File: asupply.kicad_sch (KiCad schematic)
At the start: 98 parts, among them U10 LT3081xDF, U11 LT3042xMSE, U12 LT3045xMSE, U13 LT3045xMSE, U14 LT3042xMSE, U15 LT3094xMSE, U16 LT3042xMSE, U9 LTC3261

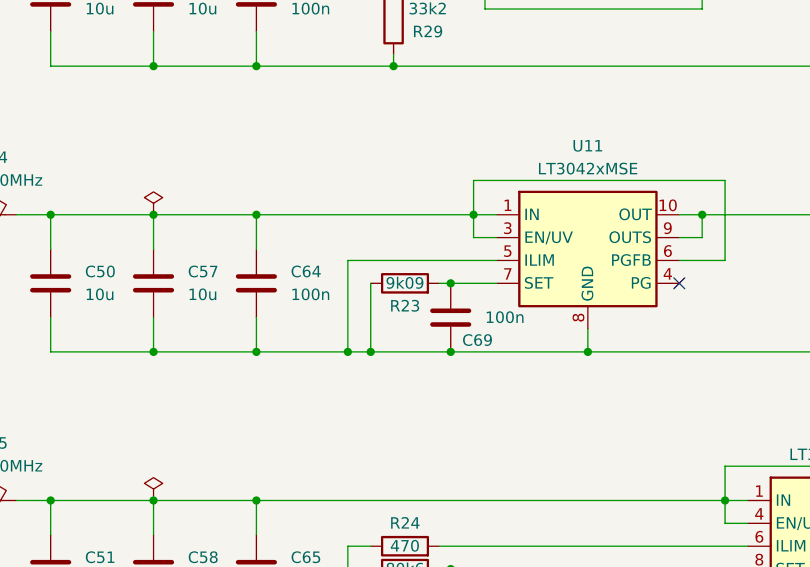
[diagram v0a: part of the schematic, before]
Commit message: sch: Fix Issue #15
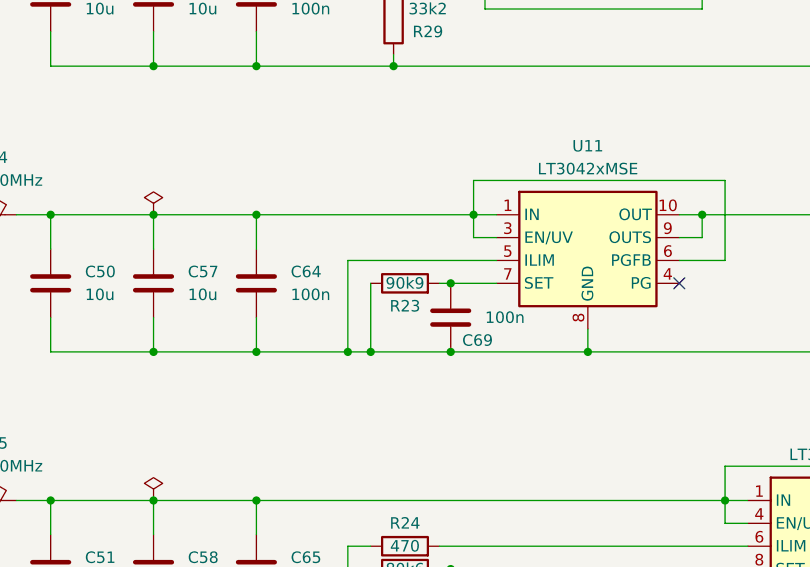
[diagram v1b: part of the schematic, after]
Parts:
- R23: value 9k09 -> 90k9; MFR_PN CR0603-FX-9091ELF -> RT0603FRE0790K9L
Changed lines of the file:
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@@
       (effects (font (size 1.27 1.27)))
     )
-    (property "Value" "9k09" (at 203.2 83.82 90)
+    (property "Value" "90k9" (at 203.2 83.82 90)
       (effects (font (size 1.27 1.27)))
     )
@@
       (effects (font (size 1.27 1.27)) hide)
     )
-    (property "MFR_PN" "CR0603-FX-9091ELF" (at 203.2 83.82 0)
+    (property "MFR_PN" "RT0603FRE0790K9L" (at 203.2 83.82 0)
       (effects (font (size 1.27 1.27)) hide)
     )

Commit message: sch: Fix Issue #14
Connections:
- net GND: now also R99.2; no longer R99.1
- net LD_EN: now also R99.1, U12.4 (EN/UV); no longer R99.2, U12.5 (PG)
- net at C51.1, C58.1, C65.1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: no longer U12.4 (EN/UV)
- no-connect marks 7 -> 8
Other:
- moved on the sheet: C51, C58, C65, C77, C84, C91, FB5

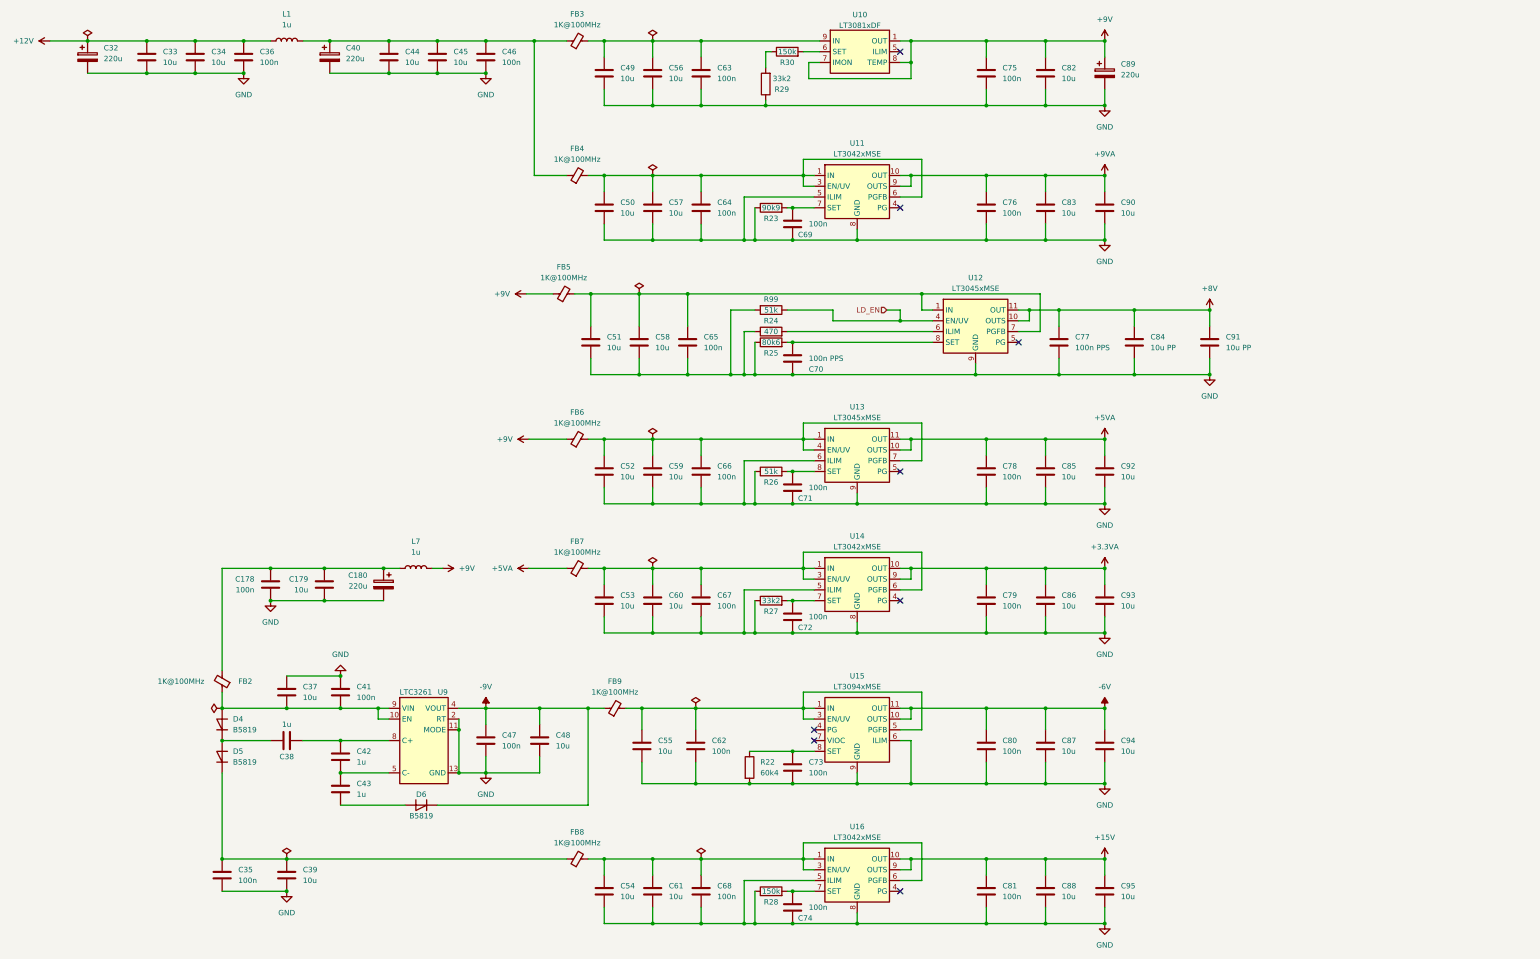
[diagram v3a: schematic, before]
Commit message: pcb: Finish Layout for rev0_3 - Assign MFR_PN for all Components - schematics changes:   - drivestage: Add Switch to optionally enable Modulation Signal Termination   -             Add alternate Precision Power Resistor   -             Modify the RC network values at TIA LPF Output   - MCU: Add Redundant 2.54mm pitch Programming Header   - thermostat: Duplicate the power filter network for alternate Temperature ADC
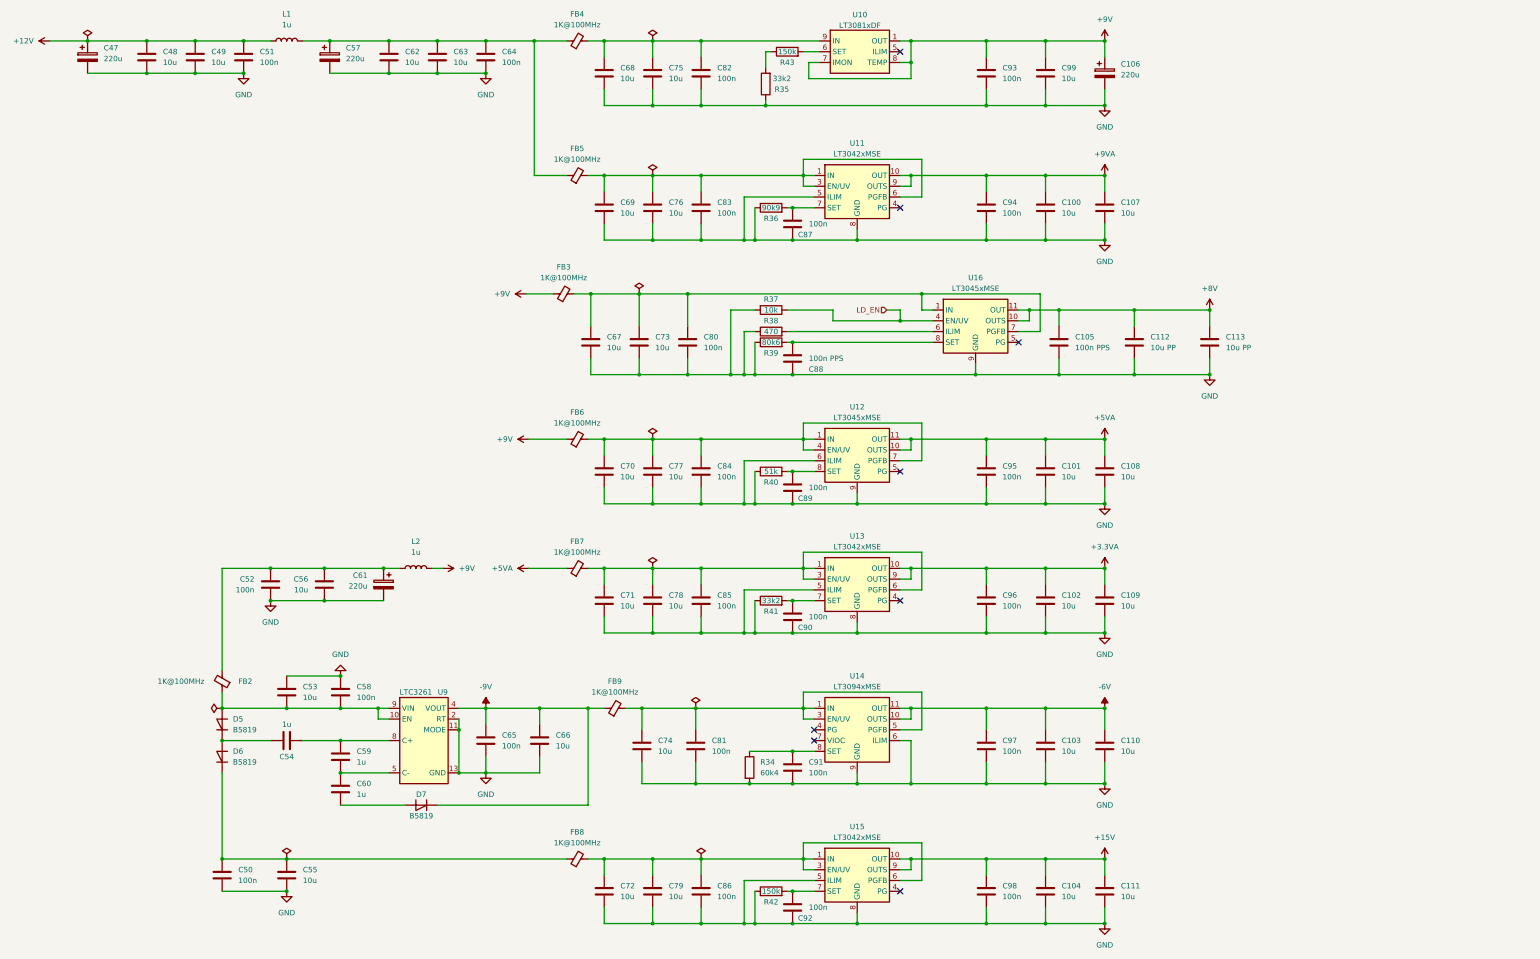
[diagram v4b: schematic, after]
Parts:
- R37: renamed from R99; value 51k -> 10k; MFR_PN RMCF0603FT51K0 -> RNCP0603FTD10K0; MFR_PN_ALT CR0603-FX-5102ELF -> RMCF0603FT10K0
- renumbered C83 to C100, C85 to C101, C86 to C102, C87 to C103, C88 to C104, C77 to C105, C89 to C106, C90 to C107, C92 to C108, C93 to C109, C94 to C110, C95 to C111, C84 to C112, C91 to C113, C32 to C47, C33 to C48, C34 to C49, C35 to C50, C36 to C51, C178 to C52, C37 to C53, C38 to C54, C39 to C55, C179 to C56, C40 to C57, C41 to C58, C42 to C59, C43 to C60, C180 to C61, C44 to C62, C45 to C63, C46 to C64, C47 to C65, C48 to C66, C51 to C67, C49 to C68, C50 to C69, C52 to C70, C53 to C71, C54 to C72, C58 to C73, C55 to C74, C56 to C75, C57 to C76, C59 to C77, C60 to C78, C61 to C79, C65 to C80, C62 to C81, C63 to C82, C64 to C83, C66 to C84, C67 to C85, C68 to C86, C69 to C87, C70 to C88, C71 to C89, C72 to C90, C73 to C91, C74 to C92, C75 to C93, C76 to C94, C78 to C95, C79 to C96, C80 to C97, C81 to C98, C82 to C99, D4 to D5, D5 to D6, D6 to D7, FB5 to FB3, FB3 to FB4, FB4 to FB5, L7 to L2, R22 to R34, R29 to R35, R23 to R36, R24 to R38, R25 to R39, R26 to R40, R27 to R41, R28 to R42, R30 to R43, U13 to U12, U14 to U13, U15 to U14, U16 to U15, U12 to U16

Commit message: sch: Update Title Block Info - rev0.3 -> rev0_3 - Correct the title of each schematics - Update the modified time
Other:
- company: M-Labs -> M-Labs Limited
- title: Kirdy -> analog supply
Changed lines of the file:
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@@
   (paper "A3")
   (title_block
-    (title "Kirdy")
-    (date "2022-07-03")
-    (rev "r0.3")
-    (company "M-Labs")
+    (title "analog supply")
+    (date "2023-11-09")
+    (rev "r0_3")
+    (company "M-Labs Limited")
     (comment 1 "Linus Woo Chun Kit")
   )

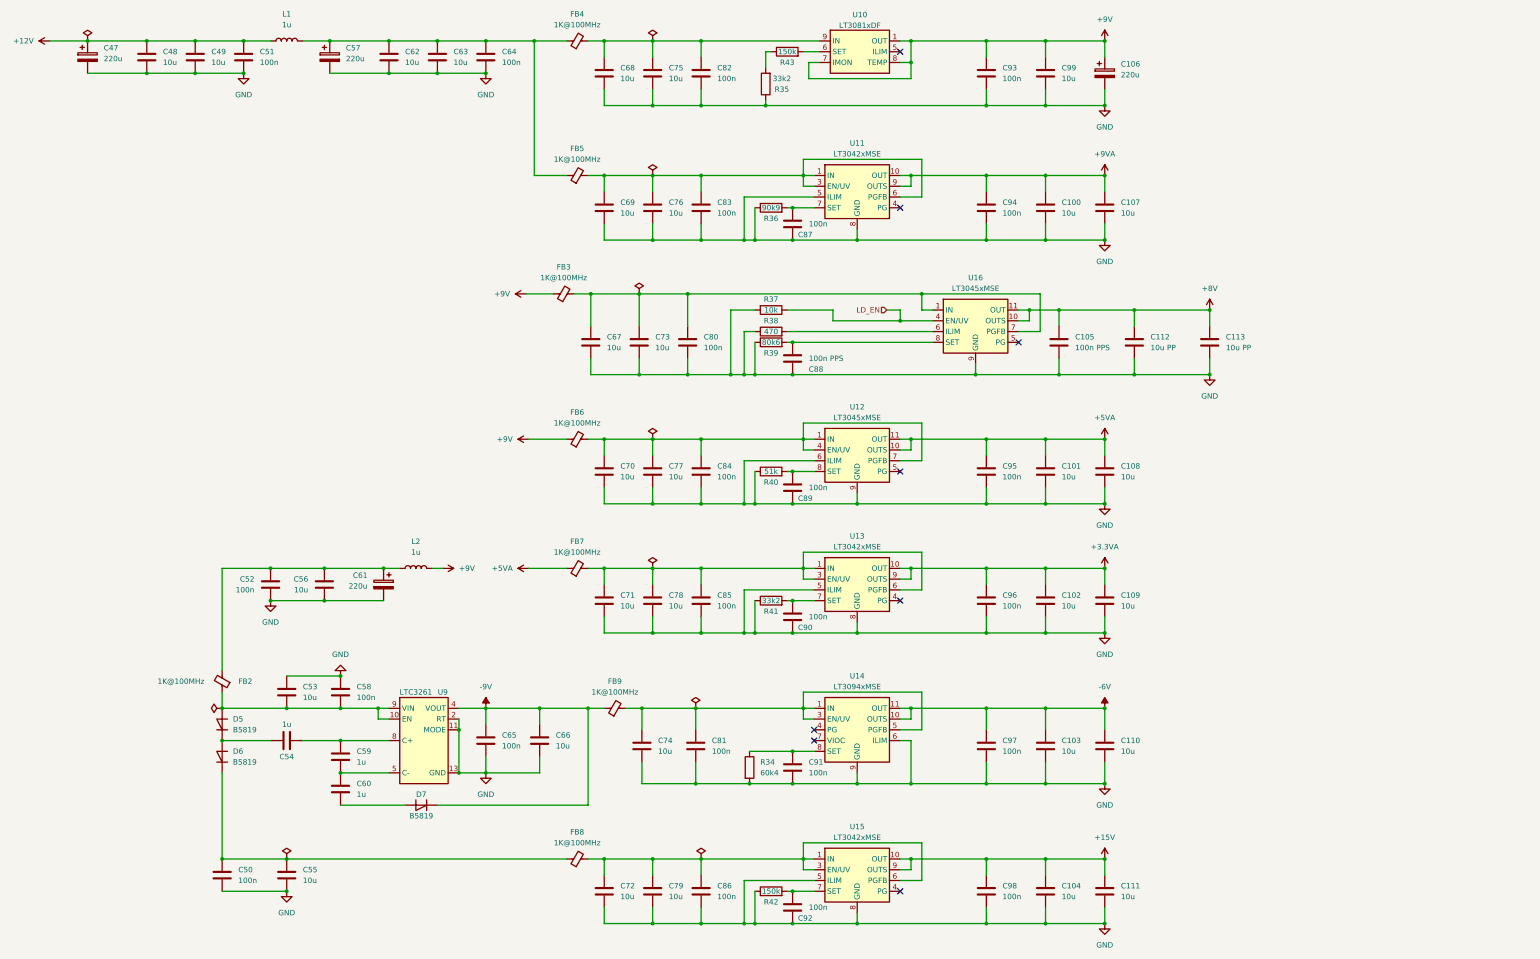
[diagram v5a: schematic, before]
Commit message: sch, pcb: Correct MFR/PN and optimize BOM
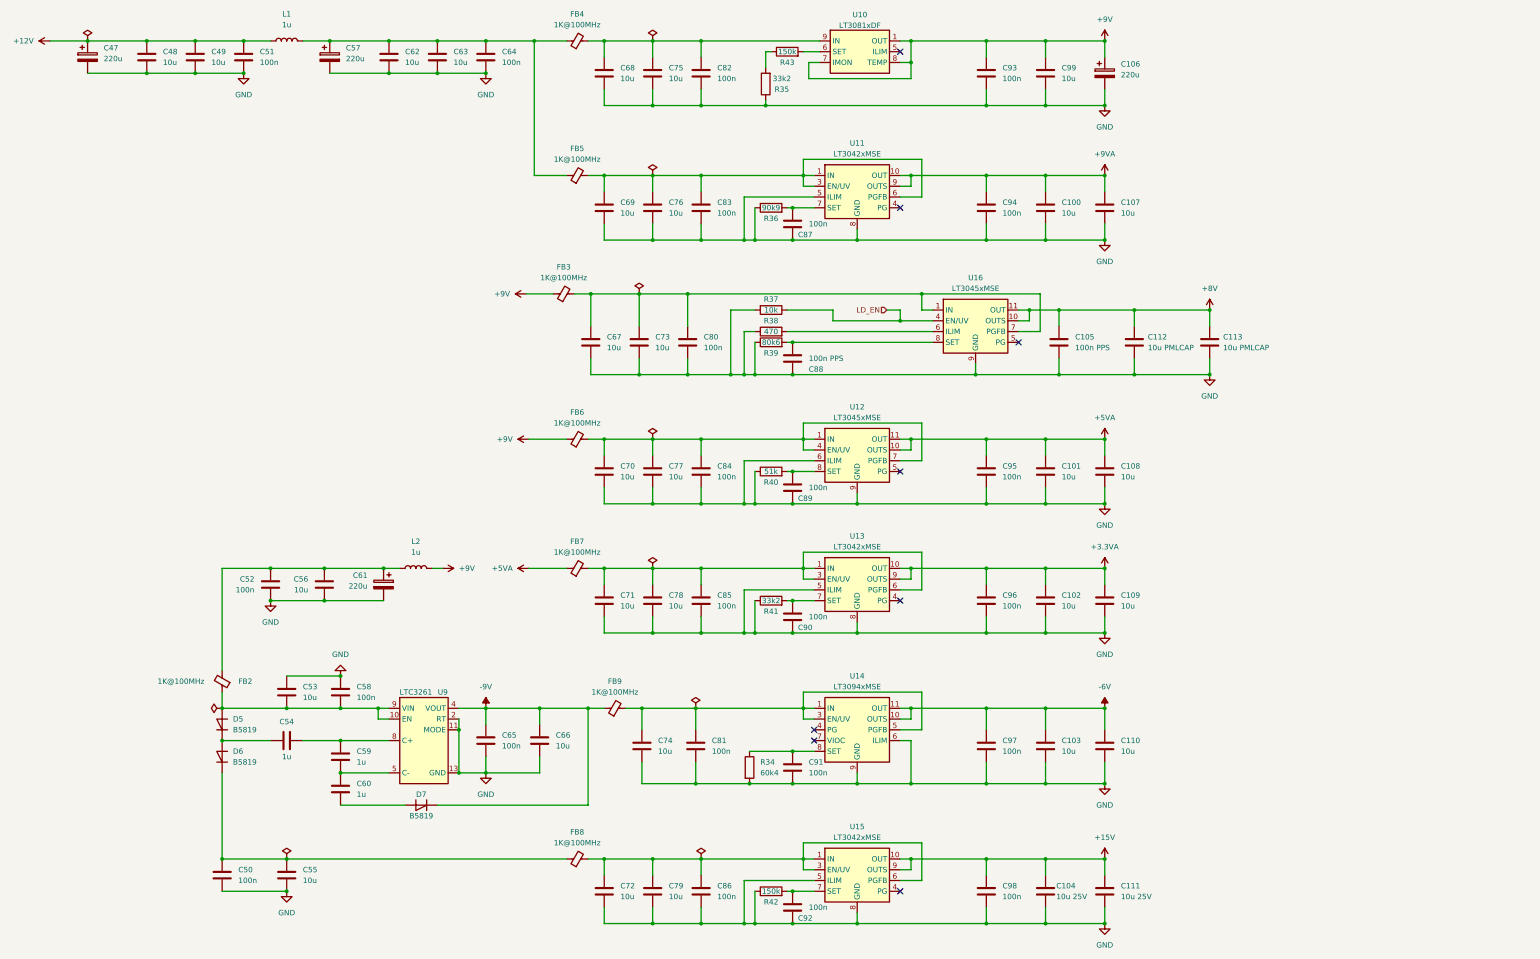
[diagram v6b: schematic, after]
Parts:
- C104, C111: value 10u -> 10u 25V; MFR_PN CL21B106KOQNNNG -> GRM21BZ71E106KE15K; MFR_PN_ALT CL21B106KOQNNNE -> GRM21BZ71E106KE15L
- C110: MFR_PN CL21B106KOQNNNG -> GRM21BZ71E106KE15K; MFR_PN_ALT CL21B106KOQNNNE -> GRM21BZ71E106KE15L
- C112, C113: value 10u PP -> 10u PMLCAP
- R36: MFR_PN_ALT RK73H1JTTD9091F -> ERJ-UP3F9092V
- U10: MFR_PN LT3081EDF -> LT3081EDF#PBF

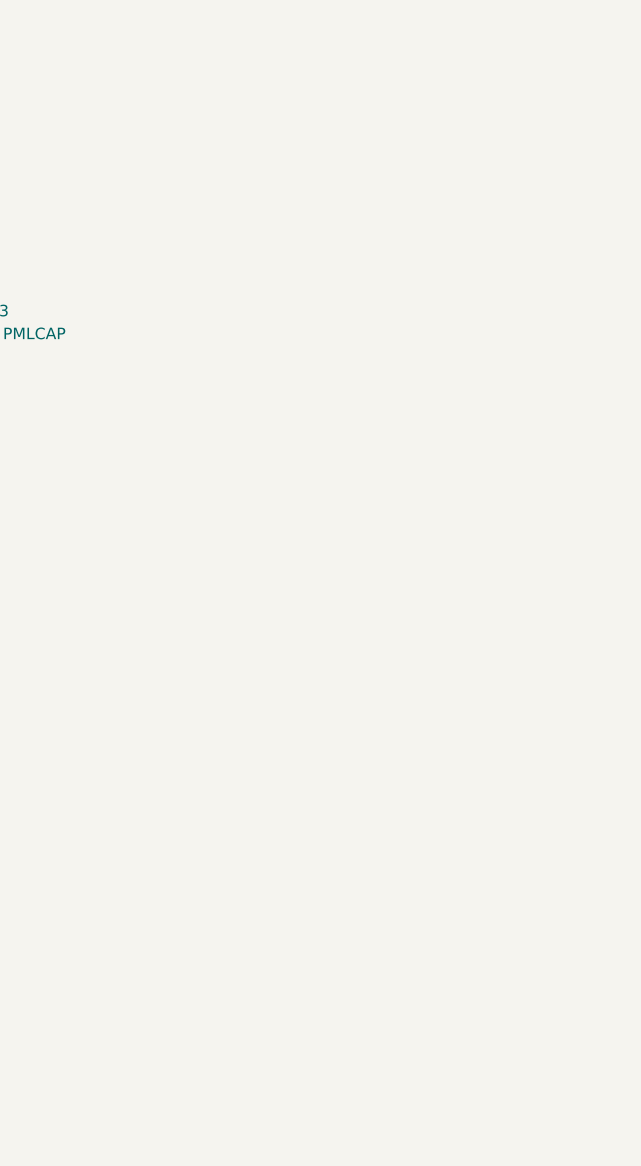
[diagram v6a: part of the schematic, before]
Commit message: sch, pcb: Add LEDs and TPs to Critical Power Rails
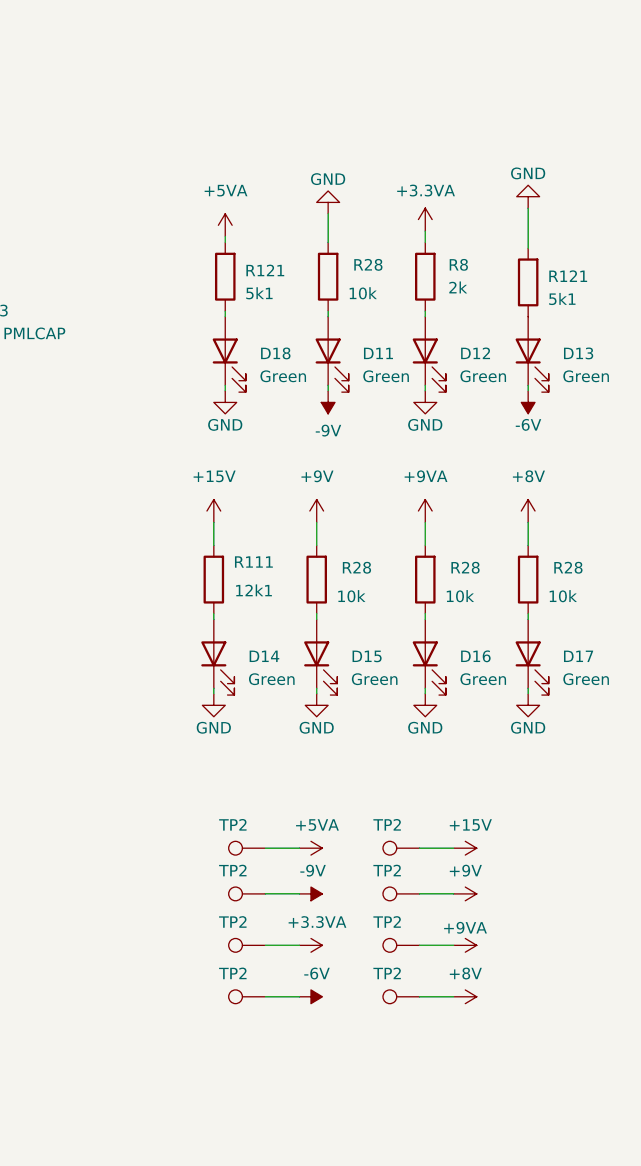
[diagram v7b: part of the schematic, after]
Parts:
- added D11, D12, D13, D14, D15, D16, D17, D18: Green, LED_SMD:LED_0603_1608Metric, symbol Device:LED
- added R111: 12k1, Resistor_SMD:R_0603_1608Metric, symbol Device:R
- added R121 (x2): 5k1, Resistor_SMD:R_0603_1608Metric, symbol Device:R
- added R28 (x4): 10k, Resistor_SMD:R_0603_1608Metric, symbol Device:R
- added R8: 2k, Resistor_SMD:R_0603_1608Metric, symbol Device:R
- added TP2 (x8): TestPoint, TestPoint:TestPoint_Pad_1.0x1.0mm, symbol Connector:TestPoint
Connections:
- net +15V: now also R111.2, TP2.1
- net +3.3VA: now also R8.2, TP2.1
- net +5VA: now also R121.2, TP2.1
- net +8V: now also R28.2, TP2.1
- net +9V: now also R28.2, TP2.1
- net +9VA: now also R28.2, TP2.1
- net -6V: now also D13.1 (K), TP2.1
- net -9V: now also D11.1 (K), TP2.1
- net GND: now also D12.1 (K), D14.1 (K), D15.1 (K), D16.1 (K), D17.1 (K), D18.1 (K), R121.2, R28.2
- new net: D11.2 (A), R28.1
- new net: D17.2 (A), R28.1
- new net: D18.2 (A), R121.1
- new net: D13.2 (A), R121.1
- new net: D16.2 (A), R28.1
- new net: D12.2 (A), R8.1
- new net: D14.2 (A), R111.1
- new net: D15.2 (A), R28.1
